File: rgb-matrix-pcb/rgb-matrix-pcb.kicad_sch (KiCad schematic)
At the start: 35 parts, among them J1 Conn_01x16_Socket, J2 Conn_01x16_Socket, J3 Conn_01x05, U1 74HC595, U2 74HC595, U3 74HC595, U4 74HC595

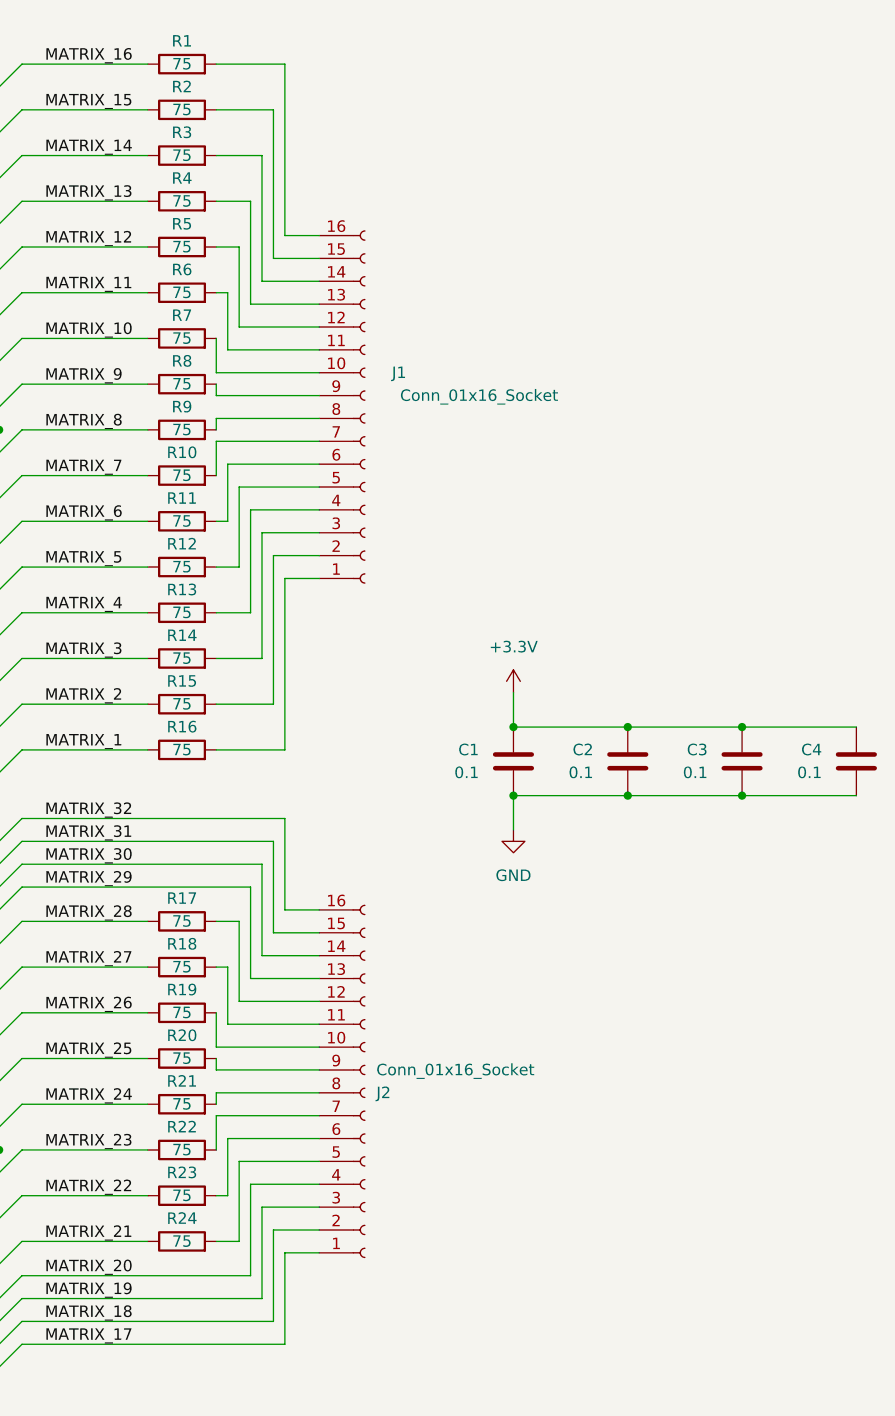
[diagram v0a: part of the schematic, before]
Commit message: Updated resistor values in schematic
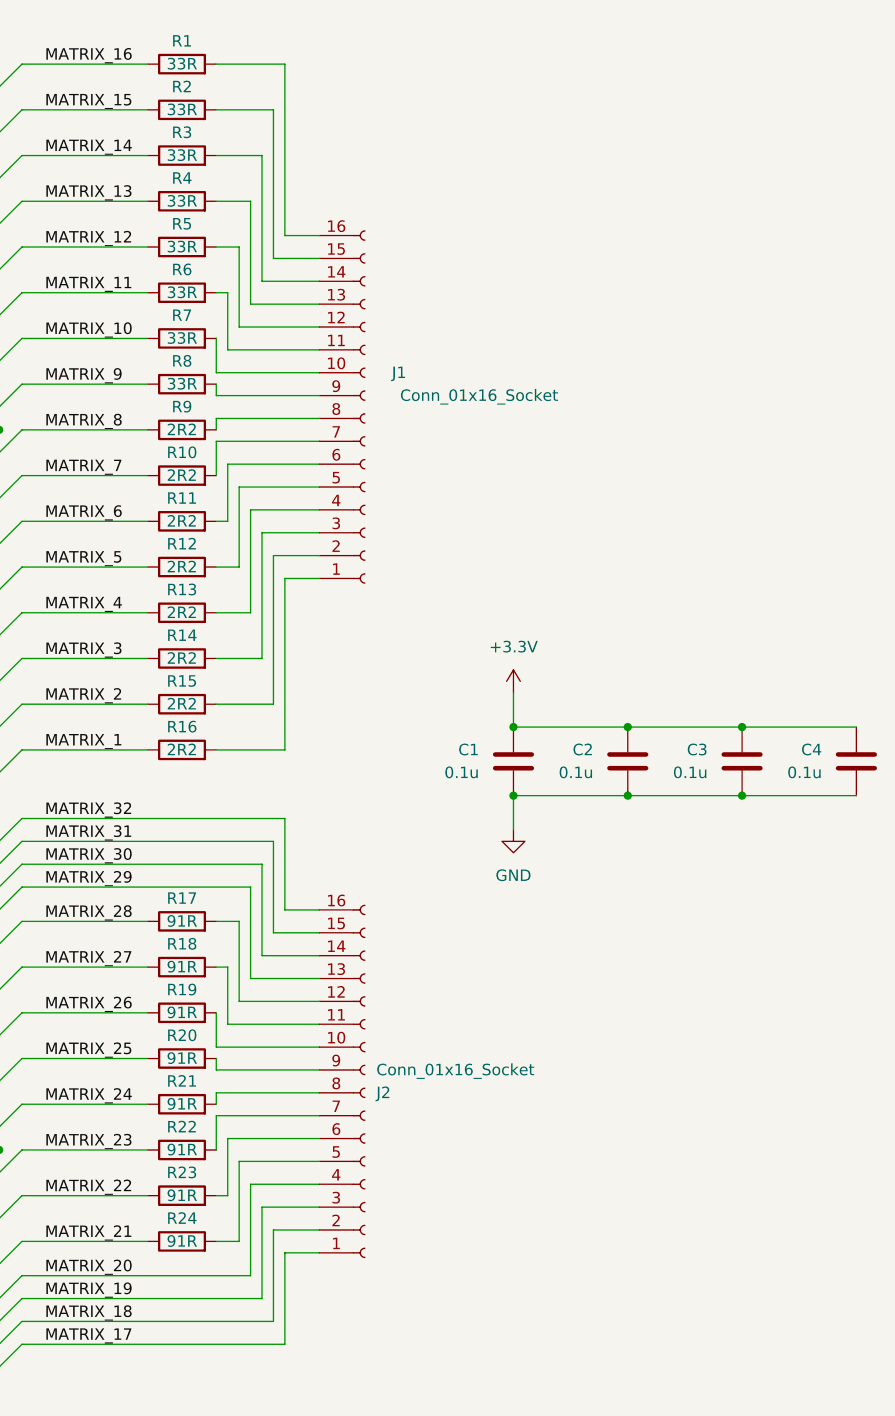
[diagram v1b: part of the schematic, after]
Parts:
- C1, C2, C3, C4: value 0.1 -> 0.1u
- R1, R2, R3, R4, R5, R6, R7, R8: value 75 -> 33R
- R10, R11, R12, R13, R14, R15, R16, R9: value 75 -> 2R2
- R17, R18, R19, R20, R21, R22, R23, R24: value 75 -> 91R
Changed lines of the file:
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@@
 			)
 		)
-		(property "Value" "75"
+		(property "Value" "2R2"
 			(at 193.04 74.93 90)
 			(effects
@@
 			)
 		)
-		(property "Value" "75"
+		(property "Value" "2R2"
 			(at 193.04 64.77 90)
 			(effects
@@
 			)
 		)
-		(property "Value" "75"
+		(property "Value" "33R"
 			(at 193.04 24.13 90)
 			(effects
@@
 			)
 		)
-		(property "Value" "75"
+		(property "Value" "91R"
 			(at 193.04 149.86 90)
 			(effects
@@
 			)
 		)
-		(property "Value" "75"
+		(property "Value" "33R"
 			(at 193.04 19.05 90)
 			(effects
@@
 			)
 		)
-		(property "Value" "75"
+		(property "Value" "33R"
 			(at 193.04 29.21 90)
 			(effects
@@
 			)
 		)
-		(property "Value" "75"
+		(property "Value" "2R2"
 			(at 193.04 95.25 90)
 			(effects
@@
 			)
 		)
-		(property "Value" "75"
+		(property "Value" "91R"
 			(at 193.04 114.3 90)
 			(effects
@@
 			)
 		)
-		(property "Value" "75"
+		(property "Value" "2R2"
 			(at 193.04 80.01 90)
 			(effects
@@
 			)
 		)
-		(property "Value" "75"
+		(property "Value" "91R"
 			(at 193.04 119.38 90)
 			(effects
@@
 			)
 		)
-		(property "Value" "75"
+		(property "Value" "33R"
 			(at 193.04 39.37 90)
 			(effects
@@
 			)
 		)
-		(property "Value" "75"
+		(property "Value" "33R"
 			(at 193.04 54.61 90)
 			(effects
@@
 			)
 		)
-		(property "Value" "75"
+		(property "Value" "91R"
 			(at 193.04 134.62 90)
 			(effects
@@
 			)
 		)
-		(property "Value" "75"
+		(property "Value" "33R"
 			(at 193.04 44.45 90)
 			(effects
@@
 			)
 		)
-		(property "Value" "75"
+		(property "Value" "91R"
 			(at 193.04 139.7 90)
 			(effects
@@
 			)
 		)
-		(property "Value" "75"
+		(property "Value" "91R"
 			(at 193.04 124.46 90)
 			(effects
@@
 			)
 		)
-		(property "Value" "75"
+		(property "Value" "33R"
 			(at 193.04 49.53 90)
 			(effects
@@
 			)
 		)
-		(property "Value" "75"
+		(property "Value" "2R2"
 			(at 193.04 69.85 90)
 			(effects
@@
 			)
 		)
-		(property "Value" "75"
+		(property "Value" "33R"
 			(at 193.04 34.29 90)
 			(effects
@@
 		(fields_autoplaced yes)
 		(property "Reference" "C3"
-			(at 251.46 95.25 0)
+			(at 251.46 95.2499 0)
 			(effects
 				(font
@@
 			)
 		)
-		(property "Value" "0.1"
-			(at 251.46 97.79 0)
+		(property "Value" "0.1u"
+			(at 251.46 97.7899 0)
 			(effects
 				(font
@@
 		(fields_autoplaced yes)
 		(property "Reference" "C1"
-			(at 226.06 95.25 0)
+			(at 226.06 95.2499 0)
 			(effects
 				(font
@@
 			)
 		)
-		(property "Value" "0.1"
-			(at 226.06 97.79 0)
+		(property "Value" "0.1u"
+			(at 226.06 97.7899 0)
 			(effects
 				(font
@@
 		(fields_autoplaced yes)
 		(property "Reference" "C2"
-			(at 238.76 95.25 0)
+			(at 238.76 95.2499 0)
 			(effects
 				(font
@@
 			)
 		)
-		(property "Value" "0.1"
-			(at 238.76 97.79 0)
+		(property "Value" "0.1u"
+			(at 238.76 97.7899 0)
 			(effects
 				(font
@@
 			)
 		)
-		(property "Value" "75"
+		(property "Value" "2R2"
 			(at 193.04 59.69 90)
 			(effects
@@
 			)
 		)
-		(property "Value" "75"
+		(property "Value" "2R2"
 			(at 193.04 90.17 90)
 			(effects
@@
 			)
 		)
-		(property "Value" "75"
+		(property "Value" "91R"
 			(at 193.04 129.54 90)
 			(effects
@@
 		(fields_autoplaced yes)
 		(property "Reference" "C4"
-			(at 264.16 95.25 0)
+			(at 264.16 95.2499 0)
 			(effects
 				(font
@@
 			)
 		)
-		(property "Value" "0.1"
-			(at 264.16 97.79 0)
+		(property "Value" "0.1u"
+			(at 264.16 97.7899 0)
 			(effects
 				(font
@@
 			)
 		)
-		(property "Value" "75"
+		(property "Value" "91R"
 			(at 193.04 144.78 90)
 			(effects
@@
 			)
 		)
-		(property "Value" "75"
+		(property "Value" "2R2"
 			(at 193.04 85.09 90)
 			(effects

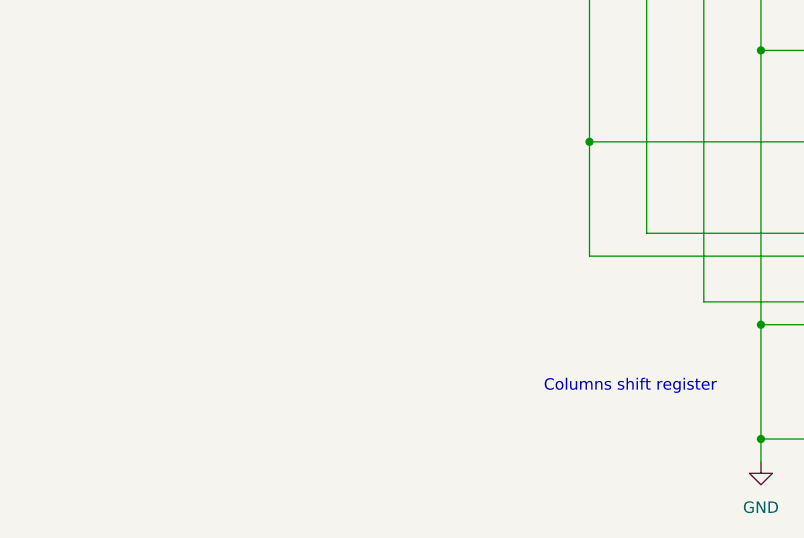
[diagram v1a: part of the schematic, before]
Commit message: Added schematic notes for greenwired current amplifiers
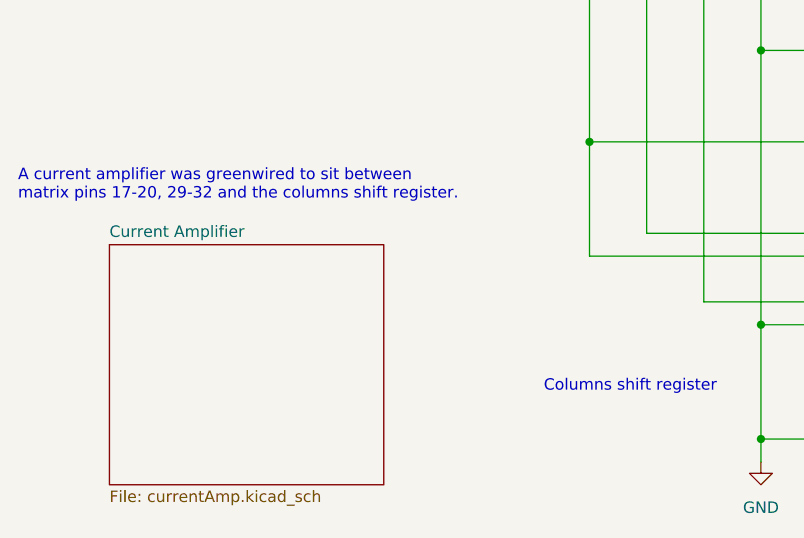
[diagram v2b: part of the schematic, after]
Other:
- added sheet Current Amplifier (currentAmp.kicad_sch)
- note added: "A current amplifier was greenwired to sit between matrix pins 17-20, 29-32 and the columns shift register."
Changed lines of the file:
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@@
 		)
 	)
+	(text "A current amplifier was greenwired to sit between\nmatrix pins 17-20, 29-32 and the columns shift register."
+		(exclude_from_sim no)
+		(at 19.05 154.686 0)
+		(effects
+			(font
+				(size 1.27 1.27)
+			)
+			(justify left)
+		)
+	)
 	(text "Columns shift register"
 		(exclude_from_sim no)
@@
 			)
 		)
-		(property "Description" ""
+		(property "Description" "Power symbol creates a global label with name \"GND\" , ground"
 			(at 101.6 185.42 0)
 			(effects
@@
 			)
 		)
-		(property "Description" ""
+		(property "Description" "Power symbol creates a global label with name \"+3.3V\""
 			(at 40.64 29.21 0)
 			(effects
@@
 			)
 		)
-		(property "Description" ""
+		(property "Description" "Power symbol creates a global label with name \"+3.3V\""
 			(at 229.87 88.9 0)
 			(effects
@@
 			)
 		)
-		(property "Description" ""
+		(property "Description" "Special symbol for telling ERC where power comes from"
 			(at 58.42 45.72 0)
 			(effects
@@
 			)
 		)
-		(property "Description" ""
+		(property "Description" "Power symbol creates a global label with name \"GND\" , ground"
 			(at 229.87 104.14 0)
 			(effects
@@
 			)
 		)
-		(property "Description" ""
+		(property "Description" "Power symbol creates a global label with name \"GND\" , ground"
 			(at 67.31 45.72 0)
 			(effects
@@
 			)
 		)
-		(property "Description" ""
+		(property "Description" "Special symbol for telling ERC where power comes from"
 			(at 40.64 30.48 0)
 			(effects
@@
 			)
 		)
-		(property "Description" ""
+		(property "Description" "Power symbol creates a global label with name \"+3.3V\""
 			(at 82.55 20.32 0)
 			(effects
@@
 				)
 			)
+		)
+	)
+	(sheet
+		(at 29.21 161.29)
+		(size 30.48 26.67)
+		(fields_autoplaced yes)
+		(stroke
+			(width 0.1524)
+			(type solid)
+		)
+		(fill
+			(color 0 0 0 0.0000)
+		)
+		(property "Sheetname" "Current Amplifier"
+			(at 29.21 160.5784 0)
+			(effects
+				(font
+					(size 1.27 1.27)
+				)
+				(justify left bottom)
+			)
+		)
+		(property "Sheetfile" "currentAmp.kicad_sch"
+			(at 29.21 188.5446 0)
+			(effects
+				(font
+					(size 1.27 1.27)
+				)
+				(justify left top)
+			)
+		)
+		(instances
+			(project "rgb-matrix-pcb"
+				(path "/d24d6f77-3b9a-4a71-af59-9eeebe23ffcf"
+					(page "2")
+				)
+			)
